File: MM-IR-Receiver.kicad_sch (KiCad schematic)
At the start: 2 parts

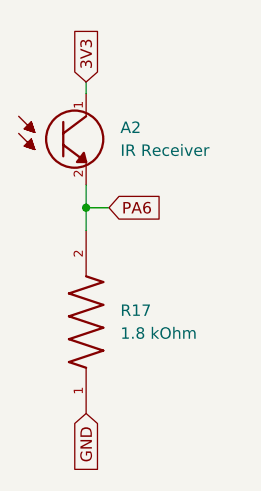
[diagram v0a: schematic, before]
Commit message: added power switch
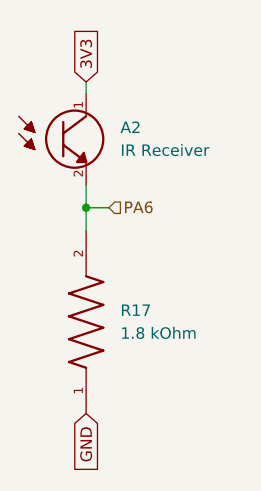
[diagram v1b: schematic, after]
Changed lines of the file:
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@@
-		)
-	)
-	(global_label "PA6"
-		(shape input)
-		(at 115.57 104.14 0)
-		(fields_autoplaced yes)
-		(effects
-			(font
-				(size 1.27 1.27)
-			)
-			(justify left)
-		)
-		(property "Intersheetrefs" "${INTERSHEET_REFS}"
-			(at 122.1233 104.14 0)
-			(effects
-				(font
-					(size 1.27 1.27)
-				)
-				(justify left)
-				(hide yes)
-			)
 		)
 	)
@@
 		)
 	)
+	(hierarchical_label "PA6"
+		(shape input)
+		(at 115.57 104.14 0)
+		(effects
+			(font
+				(size 1.27 1.27)
+			)
+			(justify left)
+		)
+	)

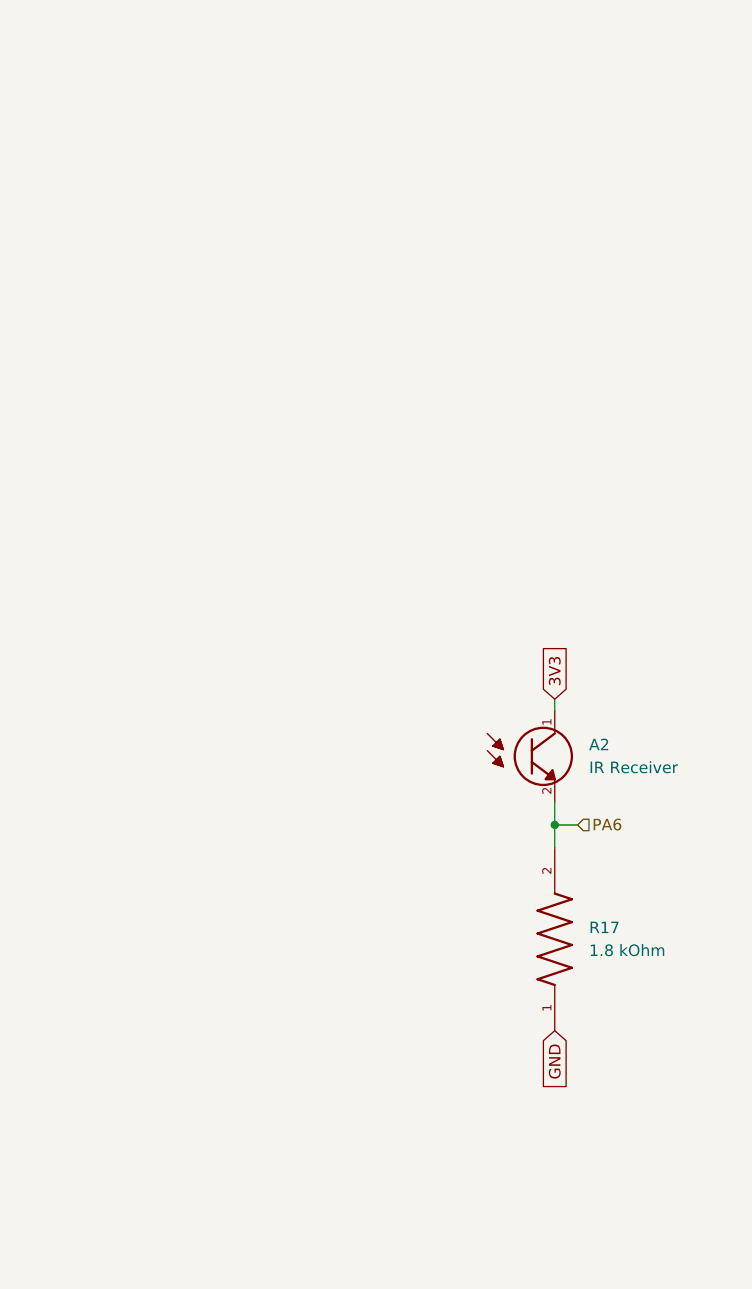
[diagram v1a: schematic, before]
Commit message: redid the 4 emitters receivers, fixed orientation of LEDS and going to continue adding footprints and replace the 60ohm resistors with 300ohm ones
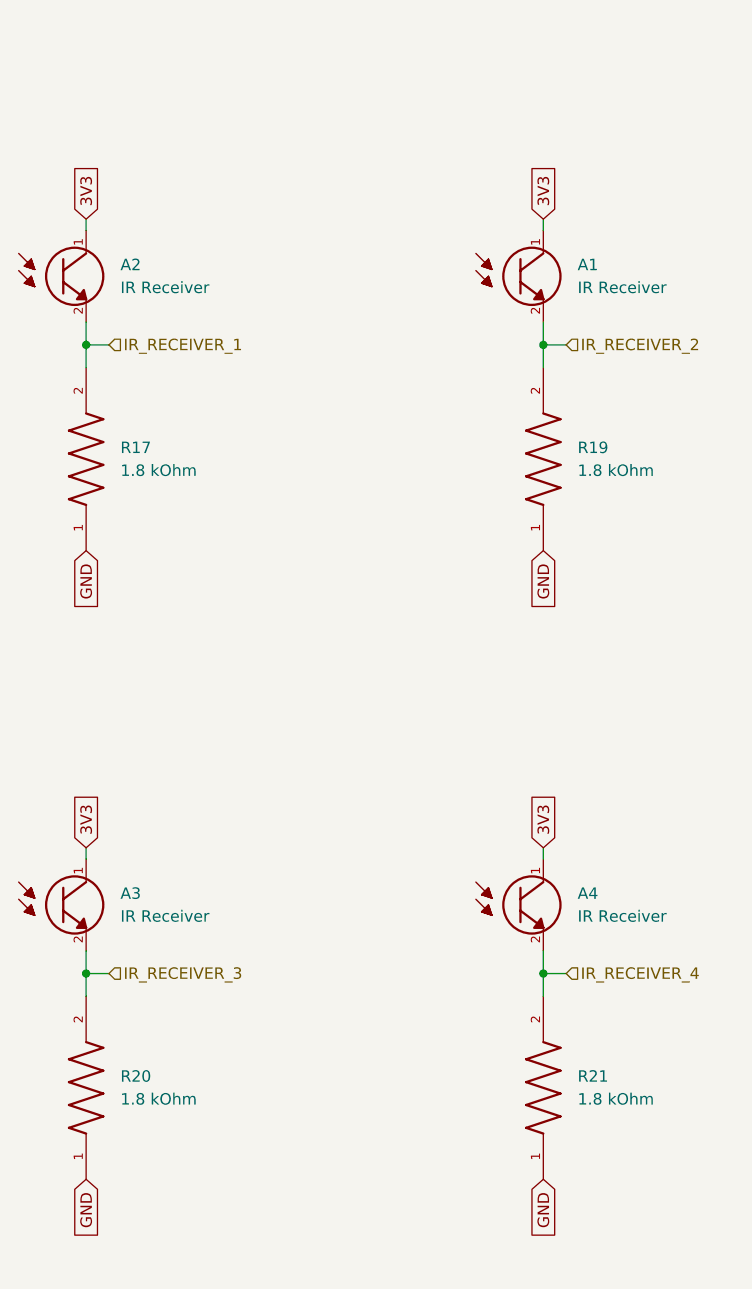
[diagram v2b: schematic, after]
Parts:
- added A1, A3, A4: IR Receiver, IR_Receiver_ALS-PT19-315C_L177_TR8:XDCR_ALS-PT19-315C_L177_TR8, symbol Phototransistor_ALS-PT19-315C_L177_TR8:ALS-PT19-315C_L177_TR8
- added R19, R20, R21: 1.8 kOhm, RMCF0805JT1K80:RESC2012X65N, symbol 1.8kOhm_RMCF0805JT1K80:RMCF0805JT1K80
- A2: footprint ALS_PT19_315C_L177_TR8:XDCR_ALS-PT19-315C_L177_TR8 -> IR_Receiver_ALS-PT19-315C_L177_TR8:XDCR_ALS-PT19-315C_L177_TR8
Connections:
- net 3V3: now also A1.1, A3.1, A4.1
- net GND: now also R19.1, R20.1, R21.1
- net PA6 renamed IR_RECEIVER_1
- new net IR_RECEIVER_2: A1.2, R19.2
- new net IR_RECEIVER_3: A3.2, R20.2
- new net IR_RECEIVER_4: A4.2, R21.2
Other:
- moved on the sheet: A2, R17

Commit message: finished adding rest of footprints, tried replacing mosfets with no success
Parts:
- R17, R19, R20, R21: footprint RMCF0805JT1K80:RESC2012X65N -> 1.8_kohm_RMCF0805JT1K80:RESC2012X65N
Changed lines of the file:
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@@
 			)
 		)
-		(property "Footprint" "RMCF0805JT1K80:RESC2012X65N"
+		(property "Footprint" "1.8_kohm_RMCF0805JT1K80:RESC2012X65N"
 			(at 111.76 133.35 0)
 			(effects
@@
 			)
 		)
-		(property "Footprint" "RMCF0805JT1K80:RESC2012X65N"
+		(property "Footprint" "1.8_kohm_RMCF0805JT1K80:RESC2012X65N"
 			(at 111.76 63.5 0)
 			(effects
@@
 			)
 		)
-		(property "Footprint" "RMCF0805JT1K80:RESC2012X65N"
+		(property "Footprint" "1.8_kohm_RMCF0805JT1K80:RESC2012X65N"
 			(at 60.96 133.35 0)
 			(effects
@@
 			)
 		)
-		(property "Footprint" "RMCF0805JT1K80:RESC2012X65N"
+		(property "Footprint" "1.8_kohm_RMCF0805JT1K80:RESC2012X65N"
 			(at 60.96 63.5 0)
 			(effects

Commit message: PCB tentative finished
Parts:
- removed A1, A2, A3, A4: IR Receiver, IR_Receiver_ALS-PT19-315C_L177_TR8:XDCR_ALS-PT19-315C_L177_TR8, symbol Phototransistor_ALS-PT19-315C_L177_TR8:ALS-PT19-315C_L177_TR8
- added Q1, Q2, Q3, Q4: IR Receiver, IR_Receiver_ul_LTR-4206E:NoneP157X157-2_LTO, symbol IR_Receiver_ul_LTR-4206E:LTR-4206E
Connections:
- net 3V3: now also Q1.2, Q2.2, Q3.2, Q4.2
- net IR_RECEIVER_1: now also Q1.1
- net IR_RECEIVER_2: now also Q2.1
- net IR_RECEIVER_3: now also Q3.1
- net IR_RECEIVER_4: now also Q4.1
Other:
- moved on the sheet: R20, R21
